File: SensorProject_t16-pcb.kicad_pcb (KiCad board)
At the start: 2 copper layers, 48.3 x 71.1 mm, 92 parts, among them J1 Conn_01x02_Pin, J10 Conn_01x02_Pin, J11 Conn_01x02_Pin, J12 Conn_01x02_Pin, J13 Conn_01x02_Pin, J14 Conn_01x02_Pin, J15 Conn_01x02_Pin, J16 Conn_01x02_Pin, J18 Conn_02x04_Top_Bottom, J2 Conn_01x02_Pin, J20 Screw_Terminal_01x02, J3 Conn_01x02_Pin, J4 Conn_01x02_Pin, J5 Conn_01x02_Pin, J6 Conn_01x02_Pin, J7 Conn_01x02_Pin, J8 Conn_01x02_Pin, J9 Conn_01x02_Pin, SW1 SW_Push, SW2 SW_Push, U1 ADS1115IDGS, U2 ADS1115IDGS, U3 ADS1115IDGS, U4 ADS1115IDGS, U5 STM32F411CEU6, U6 AMS1117-3.3 SOT-223, U7 RFM95W-915S2, Y1 25MHz, Y2 32.758kHz

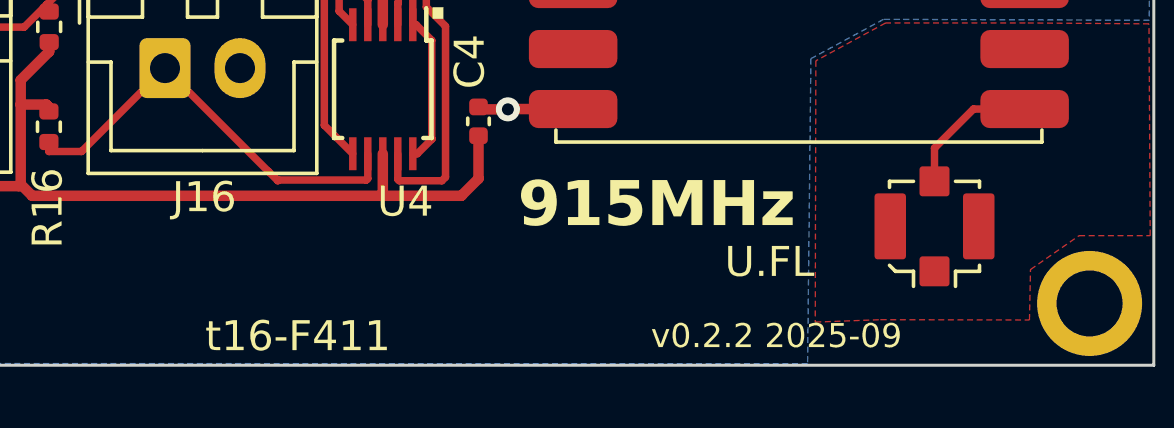
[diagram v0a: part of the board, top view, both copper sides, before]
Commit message: added new battery holder footprint.
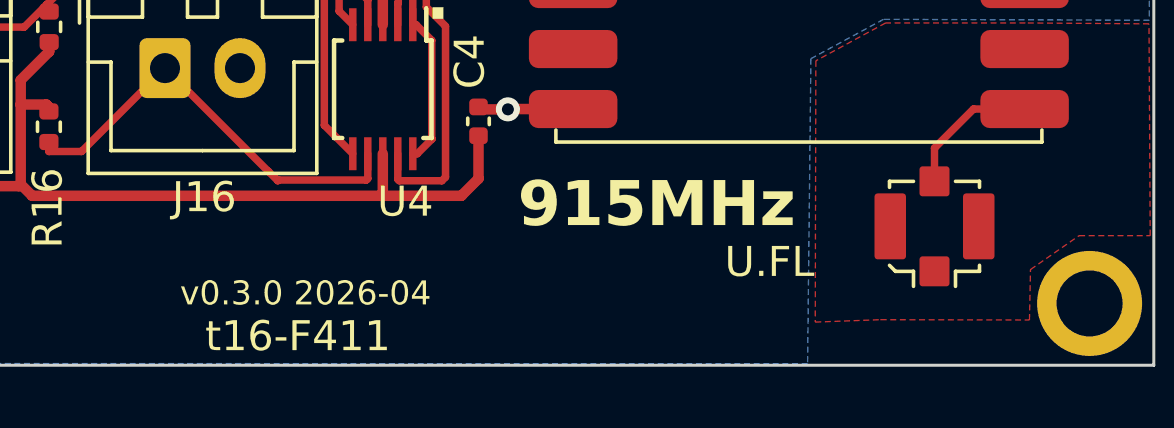
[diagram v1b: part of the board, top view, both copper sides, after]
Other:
- board text added: "v0.3.0 2026-04"
- board text removed: "v0.2.2 2025-09"

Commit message: ongoing.
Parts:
- moved NT2 1.20 mm to (85.9, 45.9)
- moved NT1 0.87 mm to (78.2, 49.1)
- moved H2 0.37 mm to (95.3, 26.5)
- moved H1 0.36 mm to (95.3, 93.0)
- moved H3 0.29 mm to (51.9, 26.5)
- moved H4 0.28 mm to (51.9, 93.0)
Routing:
- net GND_LSE: track 15.0 -> 14.5 mm
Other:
- board size 48.3 x 71.1 mm -> 48.1 x 71.1 mm
- board text added: "v0.2.2 2025-09"
- board text removed: "v0.3.0 2026-04"
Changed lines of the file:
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@@
 		(capping no)
 		(filling no)
-		(aux_axis_origin 49.65 95.19)
-		(grid_origin 49.65 95.19)
+		(aux_axis_origin 49.579997 95.199999)
+		(grid_origin 49.579997 95.199999)
 		(pcbplotparams
 			(layerselection 0x00000000_00000000_5555555f_5755f5ff)
@@
 	(footprint "ProjectLib:MountingHole_2.2mm_M2_ISO7380_Pad"
 		(layer "F.Cu")
-		(at 95.65 93.19)
+		(at 95.35 93)
 		(descr "Mounting Hole 2.2mm, M2, ISO7380")
 		(tags "mounting hole 2.2mm m2 iso7380")
@@
 	(footprint "ProjectLib:MountingHole_2.2mm_M2_ISO7380_Pad"
 		(layer "F.Cu")
-		(at 51.65 26.29)
+		(at 51.85 26.5)
 		(descr "Mounting Hole 2.2mm, M2, ISO7380")
 		(tags "mounting hole 2.2mm m2 iso7380")
@@
 	(footprint "ProjectLib:MountingHole_2.2mm_M2_ISO7380_Pad"
 		(layer "F.Cu")
-		(at 51.65 93.19)
+		(at 51.85 93)
 		(descr "Mounting Hole 2.2mm, M2, ISO7380")
 		(tags "mounting hole 2.2mm m2 iso7380")
@@
 	(footprint "ProjectLib:MountingHole_2.2mm_M2_ISO7380_Pad"
 		(layer "F.Cu")
-		(at 95.65 26.29)
+		(at 95.35 26.5)
 		(descr "Mounting Hole 2.2mm, M2, ISO7380")
 		(tags "mounting hole 2.2mm m2 iso7380")
@@
 	(footprint "ProjectLib:NetTie-2_SMD_Pad0.5mm"
 		(layer "B.Cu")
-		(at 78.92 49.46 45)
+		(at 78.15 49.06 45)
 		(descr "Net tie, 2 pin, 0.5mm square SMD pads")
 		(tags "net tie")
 		(property "Reference" "NT1"
-			(at 0 1.2 45)
+			(at 0.000001 1.2 45)
 			(layer "B.SilkS")
 			(hide yes)
@@
 		)
 		(property "Value" "NetTie_2"
-			(at 0 -1.2 45)
+			(at -0.000001 -1.2 45)
 			(layer "B.Fab")
 			(hide yes)
@@
 		(sheetname "/f411/HSE/")
 		(sheetfile "HSE.kicad_sch")
+		(zone_connect 2)
 		(attr exclude_from_pos_files exclude_from_bom allow_missing_courtyard)
 		(net_tie_pad_groups "1, 2")
@@
 	(footprint "ProjectLib:NetTie-2_SMD_Pad0.5mm"
 		(layer "B.Cu")
-		(at 85.03 46.74 135)
+		(at 85.92 45.93 135)
 		(descr "Net tie, 2 pin, 0.5mm square SMD pads")
 		(tags "net tie")
@@
 		(sheetname "/f411/LSE/")
 		(sheetfile "LSE.kicad_sch")
+		(zone_connect 2)
 		(attr exclude_from_pos_files exclude_from_bom allow_missing_courtyard)
 		(net_tie_pad_groups "1, 2")
@@
 	)
 	(gr_rect
-		(start 49.53 24.13)
-		(end 97.79 95.25)
+		(start 49.53 24.15)
+		(end 97.63 95.25)
 		(stroke
 			(width 0.1)
-			(type default)
+			(type solid)
 		)
 		(fill no)
 		(layer "Edge.Cuts")
 	)
-	(gr_text "v0.3.0 2026-04"
-		(at 65.33 93.32 0)
+	(gr_text "b2 BT1"
+		(at 74.84 57.61 0)
 		(layer "F.SilkS")
 		(effects
@@
 		)
 	)
-	(gr_text "b2 BT1"
-		(at 74.84 57.61 0)
+	(gr_text "b9"
+		(at 80.7 69.16 0)
 		(layer "F.SilkS")
 		(effects
@@
 		)
 	)
-	(gr_text "b9"
-		(at 80.7 69.16 0)
+	(gr_text "v0.2.2 2025-09"
+		(at 81.026 94.742 0)
 		(layer "F.SilkS")
 		(effects
@@
 		)
 	)
+	(point
+		(at 49.6 95.19)
+		(size 1)
+		(layer "F.Cu")
+	)
 	(segment
 		(start 93.09 40.8525)
@@
 	)
 	(segment
-		(start 84.676447 46.386447)
-		(end 84.676447 45.836447)
-		(width 0.5)
-		(layer "B.Cu")
-		(net "GND_LSE")
-	)
-	(segment
 		(start 84.676447 45.836447)
 		(end 84.61 45.77)
@@
 		)
 		(min_thickness 0.25)
-		(fill yes
+		(fill
 			(thermal_gap 0.5)
 			(thermal_bridge_width 0.5)
@@
 		(polygon
 			(pts
-				(xy 88.685262 93.731638) (xy 93.645262 93.741638) (xy 93.68 92.06) (xy 95.3 90.93) (xy 97.67 90.93)
-				(xy 97.63 83.87) (xy 93.51 83.84) (xy 88.85 83.84) (xy 86.525262 85.101638) (xy 86.505262 93.811638)
-				(xy 88.675262 93.731638)
+				(xy 88.415659 93.782132) (xy 93.375659 93.792132) (xy 93.410397 92.110494) (xy 95.030397 90.980494)
+				(xy 97.400397 90.980494) (xy 97.4 83.89) (xy 87.729997 83.890494) (xy 86.35 85.14) (xy 86.235659 93.862132)
+				(xy 88.405659 93.782132)
 			)
 		)
@@
 		)
 		(min_thickness 0.25)
-		(fill yes
+		(fill
 			(thermal_gap 0.5)
 			(thermal_bridge_width 0.5)
@@
 		(polygon
 			(pts
-				(xy 97.69 24.35) (xy 97.753 36.703) (xy 97.64 83.75) (xy 88.78 83.72) (xy 86.36 85.03) (xy 86.25 95.2)
-				(xy 49.65 95.19) (xy 49.574 25.814) (xy 49.58 24.26)
+				(xy 96.579997 25.199999) (xy 96.579997 83.55) (xy 86.879995 83.55) (xy 85.579997 84.199999) (xy 85.579997 94.199999)
+				(xy 50.579997 94.249999) (xy 50.579997 25.199999)
 			)
 		)

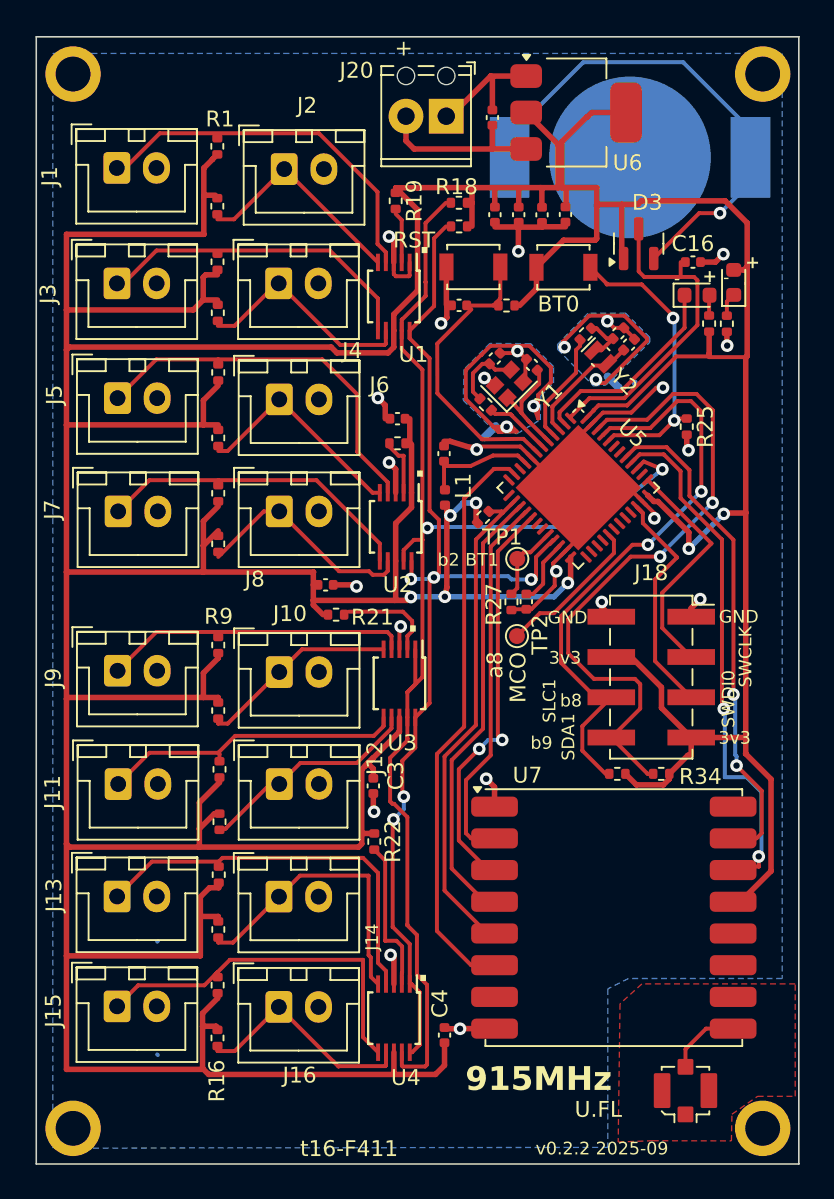
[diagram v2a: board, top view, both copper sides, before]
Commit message: added gnd-radio and gnd-ant zones on two layers. ERC and DRC mostly good. (Two warnings about pads field in NetTie footprints.)
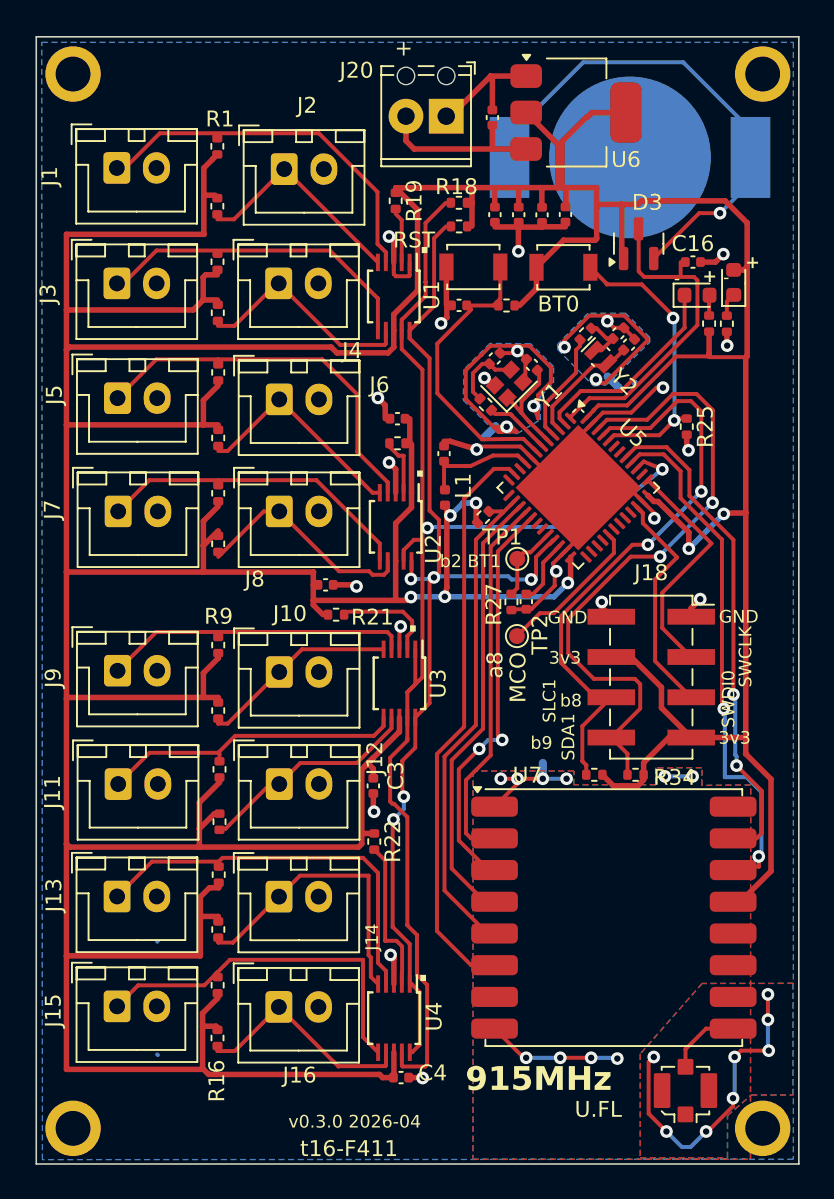
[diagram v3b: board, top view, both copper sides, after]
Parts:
- added NT3: NetTie_2, ProjectLib:NetTie-2_SMD_Pad0.5mm, B.Cu at (81.5, 70.4)
- moved C4 3.83 mm to (72.5, 89.8), turned to 0 degrees
- moved R34 1.62 mm to (87.3, 70.7)
- moved R33 1.45 mm to (84.7, 70.7)
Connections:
- U7 pad 1: GND -> GND_RADIO
- U7 pad 8: GND -> GND_RADIO
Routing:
- net GND_ANT: track 0.00 -> 20.1 mm, vias 0 -> 8
- net GND_RADIO: track 0.00 -> 17.1 mm, vias 0 -> 10
- net GND: track 68.2 -> 64.7 mm, vias 20 -> 19
- net +3V3: track 428.0 -> 424.4 mm
- net SDA1: track 41.9 -> 41.1 mm
- net SCL1: track 36.9 -> 36.3 mm
- net GND_LSE: track 14.5 -> 14.0 mm
- added copper zone on B.Cu, net GND_ANT
- added copper zone on B.Cu, net GND_RADIO
- added copper zone on F.Cu, net GND_RADIO
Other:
- board text added: "v0.3.0 2026-04"
- board text removed: "v0.2.2 2025-09"

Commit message: added caps to radio_gnd.
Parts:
- added C18: 10uF, ProjectLib:C_0402_1005Metric, F.Cu at (88.3, 70.6)
- added C19: 100nF, ProjectLib:C_0402_1005Metric, F.Cu at (91.5, 70.6)
- C1, C2, C3, C4: value 0.1µF -> 100nF
- moved R34 0.95 mm to (86.4, 70.6)
- moved R33 0.25 mm to (84.5, 70.6)
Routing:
- net +3V3: track 424.4 -> 427.1 mm
- net GND_RADIO: track 17.1 -> 19.4 mm, vias 10 -> 9

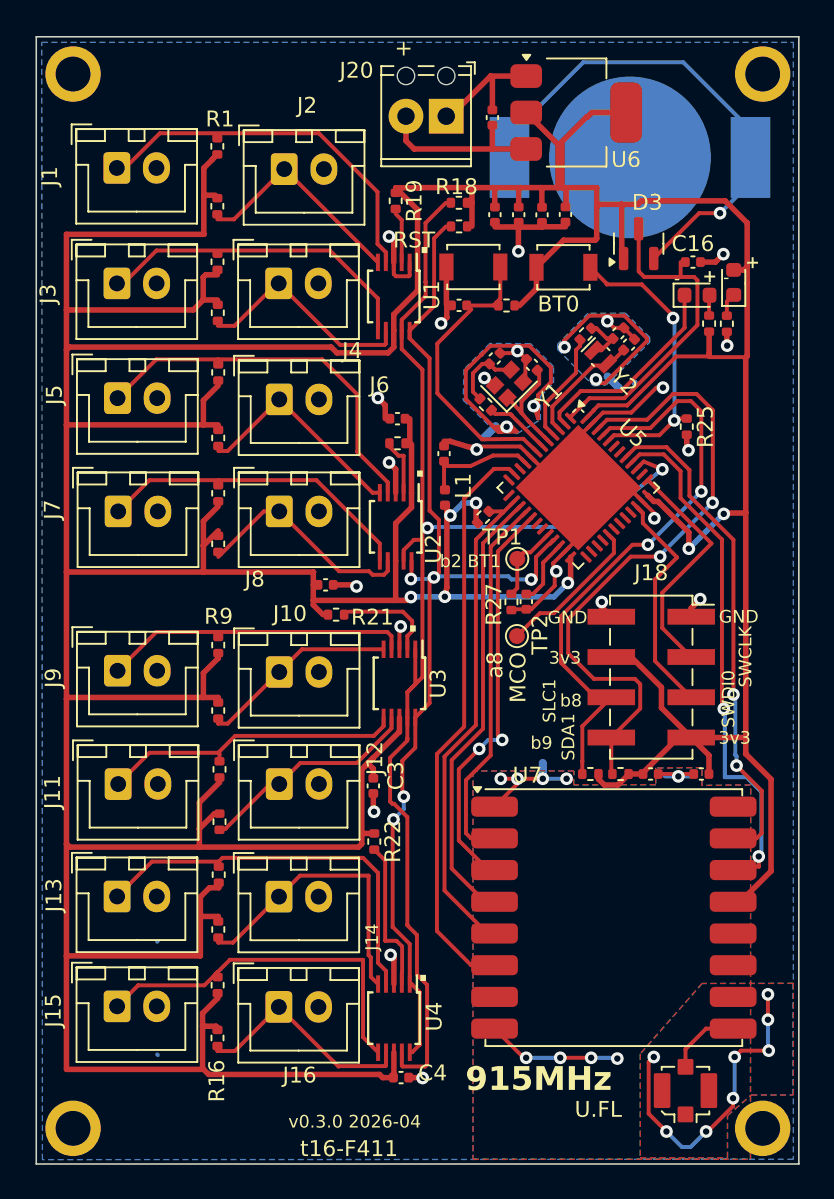
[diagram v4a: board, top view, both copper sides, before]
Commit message: added ID white space and QR code.
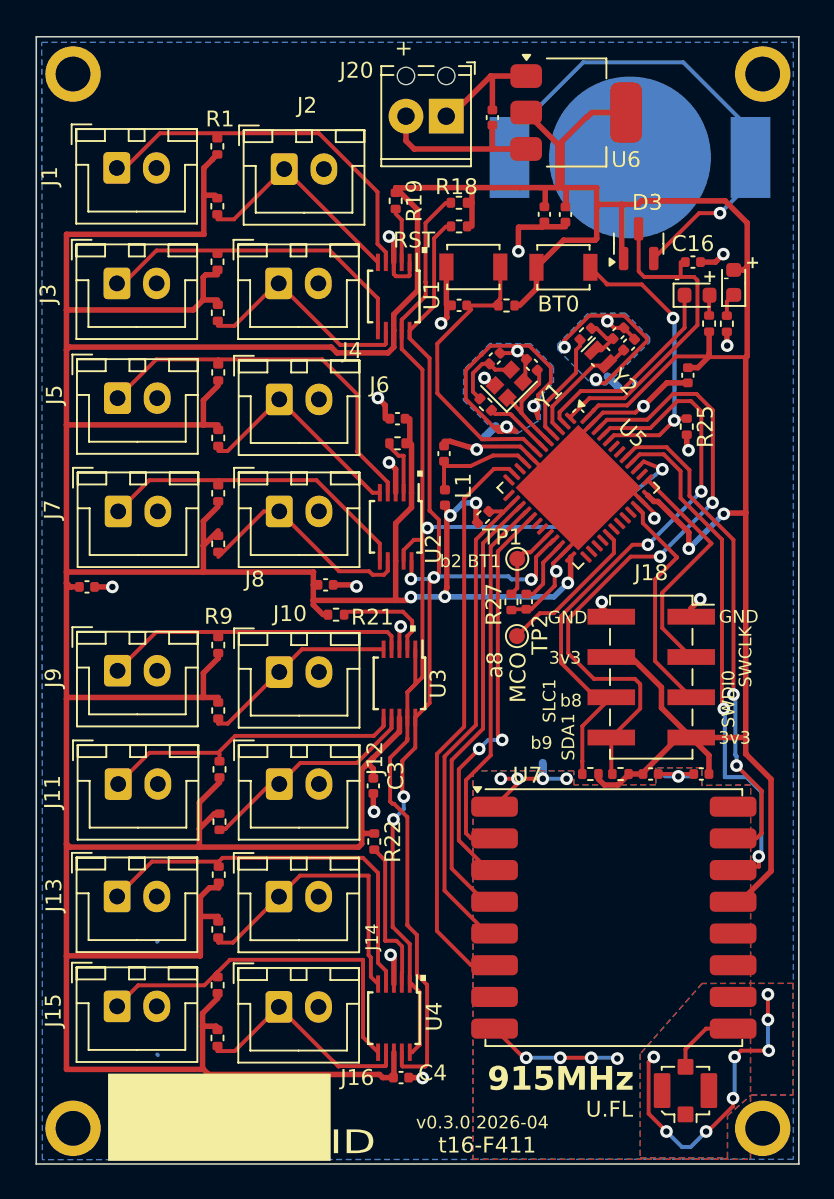
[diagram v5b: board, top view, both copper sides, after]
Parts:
- added G***: LOGO, ProjectLib:SensorProject_IDblock, F.Cu at (58.6, 92.3)
- added G***: LOGO, ProjectLib:SensorProject_QR, B.Cu at (86.0, 79.7)
- moved C8 34.8 mm to (52.7, 58.8), turned to 0 degrees
- moved C6 13.7 mm to (90.6, 45.5)
- moved C7 1.62 mm to (81.6, 35.3)
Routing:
- net GND: track 64.7 -> 66.0 mm, vias 19 -> 20

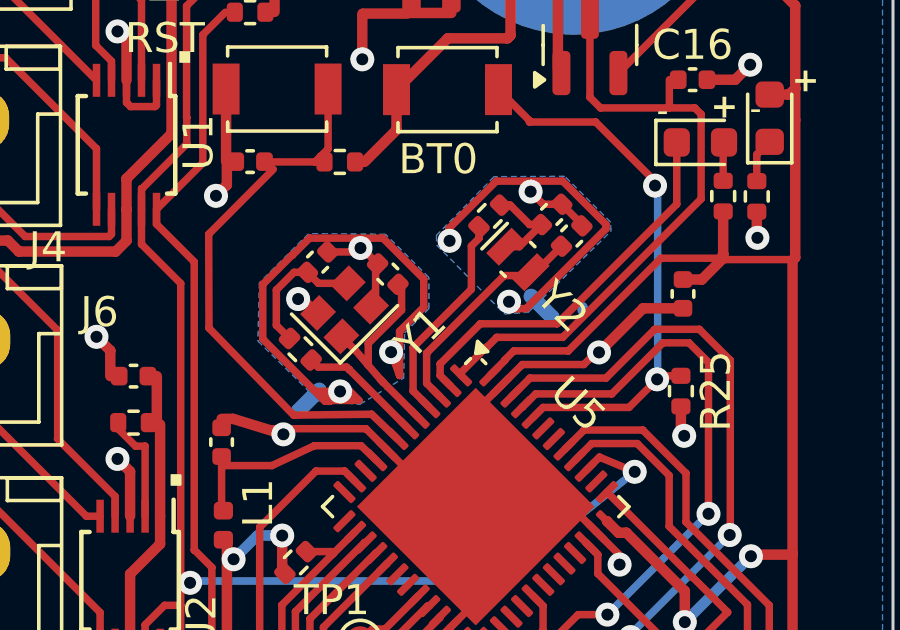
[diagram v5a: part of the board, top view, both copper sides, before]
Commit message: 3dmodels converted from .wrl to .step because .wrl seem to be missing in kicad 10.
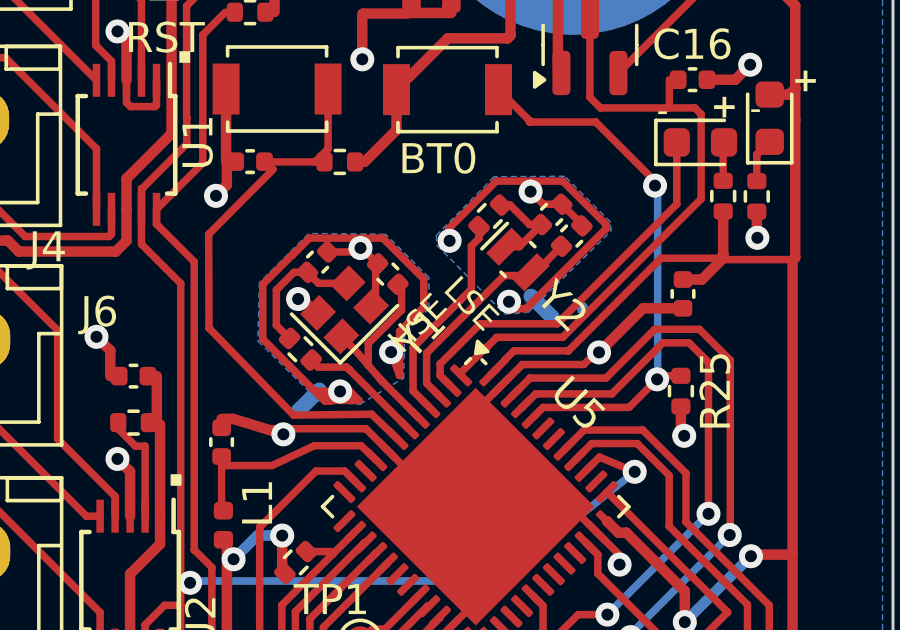
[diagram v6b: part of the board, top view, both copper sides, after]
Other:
- board text added: "HSE"
- board text added: "LSE"

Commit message: Cleaned up v0.3.0 2026-04. LSE and HSE populated.
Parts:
- moved C9 1.12 mm to (76.8, 42.0)
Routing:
- net GND: track 66.0 -> 67.1 mm
- net +3V3: track 427.2 -> 426.5 mm
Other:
- board text added: "+ 5v -"
- board text added: "A"
- board text added: "K"
- board text removed: "+"
- board text removed: "-"
